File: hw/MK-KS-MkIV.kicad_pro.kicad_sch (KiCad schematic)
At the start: 88 parts, among them J1 MuKOB IF, J10 LOOP_CUR_LIMIT, J4 COMM-DCE-10, J5 RPi-GPIO40, J6 I2C Disp, J7 KEY-PADDLE, J8 LOOP PWR, J9 SNDR/KOB, Q1 G01N20LE, Q2 MMBT3904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

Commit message: Update manual. Add IF-MkIV.
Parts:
- removed D2 (x2): 1N4007, Diode_THT:D_DO-41_SOD81_P10.16mm_Horizontal, symbol Diode:1N4004
- removed Q3: 2N3904, Package_TO_SOT_THT:TO-92_Inline, symbol Transistor_BJT:2N3904
- removed Q3: MMBT3904, Package_TO_SOT_SMD:SOT-23, symbol Transistor_BJT:MMBT3904
- removed R2: 1k, Resistor_SMD:R_0805_2012Metric_Pad1.20x1.40mm_HandSolder, symbol Device:R_US
- added BT1: Battery_Cell, symbol Device:Battery_Cell
- added C7: 10uf Tant, Capacitor_Tantalum_SMD:CP_EIA-3528-12_Kemet-T_Pad1.50x2.35mm_HandSolder, symbol Device:C_Polarized_US
- added D1: HDS20M, AES_Library:AES-BridgeRect-HDS20M-13-1KV-2A, symbol Diode_Bridge:MB2S
- added D9: MBR180S1, Diode_SMD:D_SOD-123, symbol Diode:MBR0580
- added J7: KEY-PADDLE-1_8, AES_Library:CUI_SJ1-3534NG-audio-jack, symbol AES_Library:CUI_SJ1-3534NG-audio-jack
- added JP10: EX-PWR, Connector_PinHeader_2.54mm:PinHeader_1x02_P2.54mm_Vertical, symbol Jumper:Jumper_2_Open
- C10, C11, C12, C13, C8, C9, D3: Power (none) -> 100V
- C7: Power (none) -> 80V
- D5: Power (none) -> 1KV
- JP9: value KeyJack-NP -> Shield_GND
- R2: value 0 -> 0|16
- RLY1: renamed from MS1; value RELAY-3V-DPST -> RELAY-5v|3v-DPST
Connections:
- net SEB is gone; now on net SLG-C: SW4.3
- net +3.3V: no longer R2.1
- net +5V: now also D4.1 (K), R2.1, C7.1
- net GND: now also C7.2, D1.4 (-), J7.1, JP10.2 (B)
- net KEY_PDL-: now also J7.2
- net KOB_KEY-: now also J7.4
- net LOOP_PWR: now also D1.3 (+), JP10.1 (A)
- net LP2: now also D9.2 (A); no longer D4.2 (A)
- net PDL_DASH-: now also J7.3
- net SEL: now also LED1.1 (K), SW4.1; no longer R2.1, SW4.4
- net SNDR_EN: now also R2.1; no longer SW4.1, SW4.2
- net at Q1.3 (D): now also D9.1 (K); no longer D4.1 (K)
- net at U5.1 (SND): now also BT1.1 (+)
- net SLG-C: now reaches Q2.3 (C)
- net SLG-C: now also SW4.4; no longer LED1.1 (K)
- net SER: now reaches RLY1.A1
- net SER: now also D4.2 (A), SW4.2
- net LPI+ renamed LPI_A
- net LPI_A: now also D1.2
- net LPI- renamed LPI_B
- net LPI_B: now also D1.1
- no-connect marks 38 -> 39
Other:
- note added: "1/8in Key/Paddle Jack (Same as ICOM IC-9700)"
- note added: "FOR EXTERNALLY POWERED LOOP JUMPER JP10 (LOOP PWR)"
- note added: "IF EXTERNALLY POWERED - +"
- note added: "J3 (1/4in) or J7 (1/8in) are installed They occupy the same board area."
- note added: "Key/Paddle - Sounder Mini-Test"
- note added: "Normally connected. Remove to use the 'Test Key/Closer' (or keep external key open)"
- note added: "Use when J3/J7 not installed"
- note removed: "+ EXTERNALLY POWERED"
- note removed: "EXTERNALLY POWERED -"
- note removed: "FOR EXTERNALLY POWERED LOOP JUMPER J2 (LOOP PWR)"
- note removed: "Key/Paddle - Sounder DEBUG Remove JP2 to use."
- note removed: "Normally connected. Remove to use the 'Test Key/Closer'"
- note removed: "Use when J3 not installed"
- title: MuKOB / RPi / USB - KOB/Key/Paddle&Sounder IF MkIII -> MuKOB / RPi / USB - KOB/Key/Paddle&Sounder IF MkIV
- moved on the sheet: D4, J1, J8, JP7, LED1, M_KSI1, M_KSI2, M_KSI3, M_KSI4, OP1, Q2, R2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

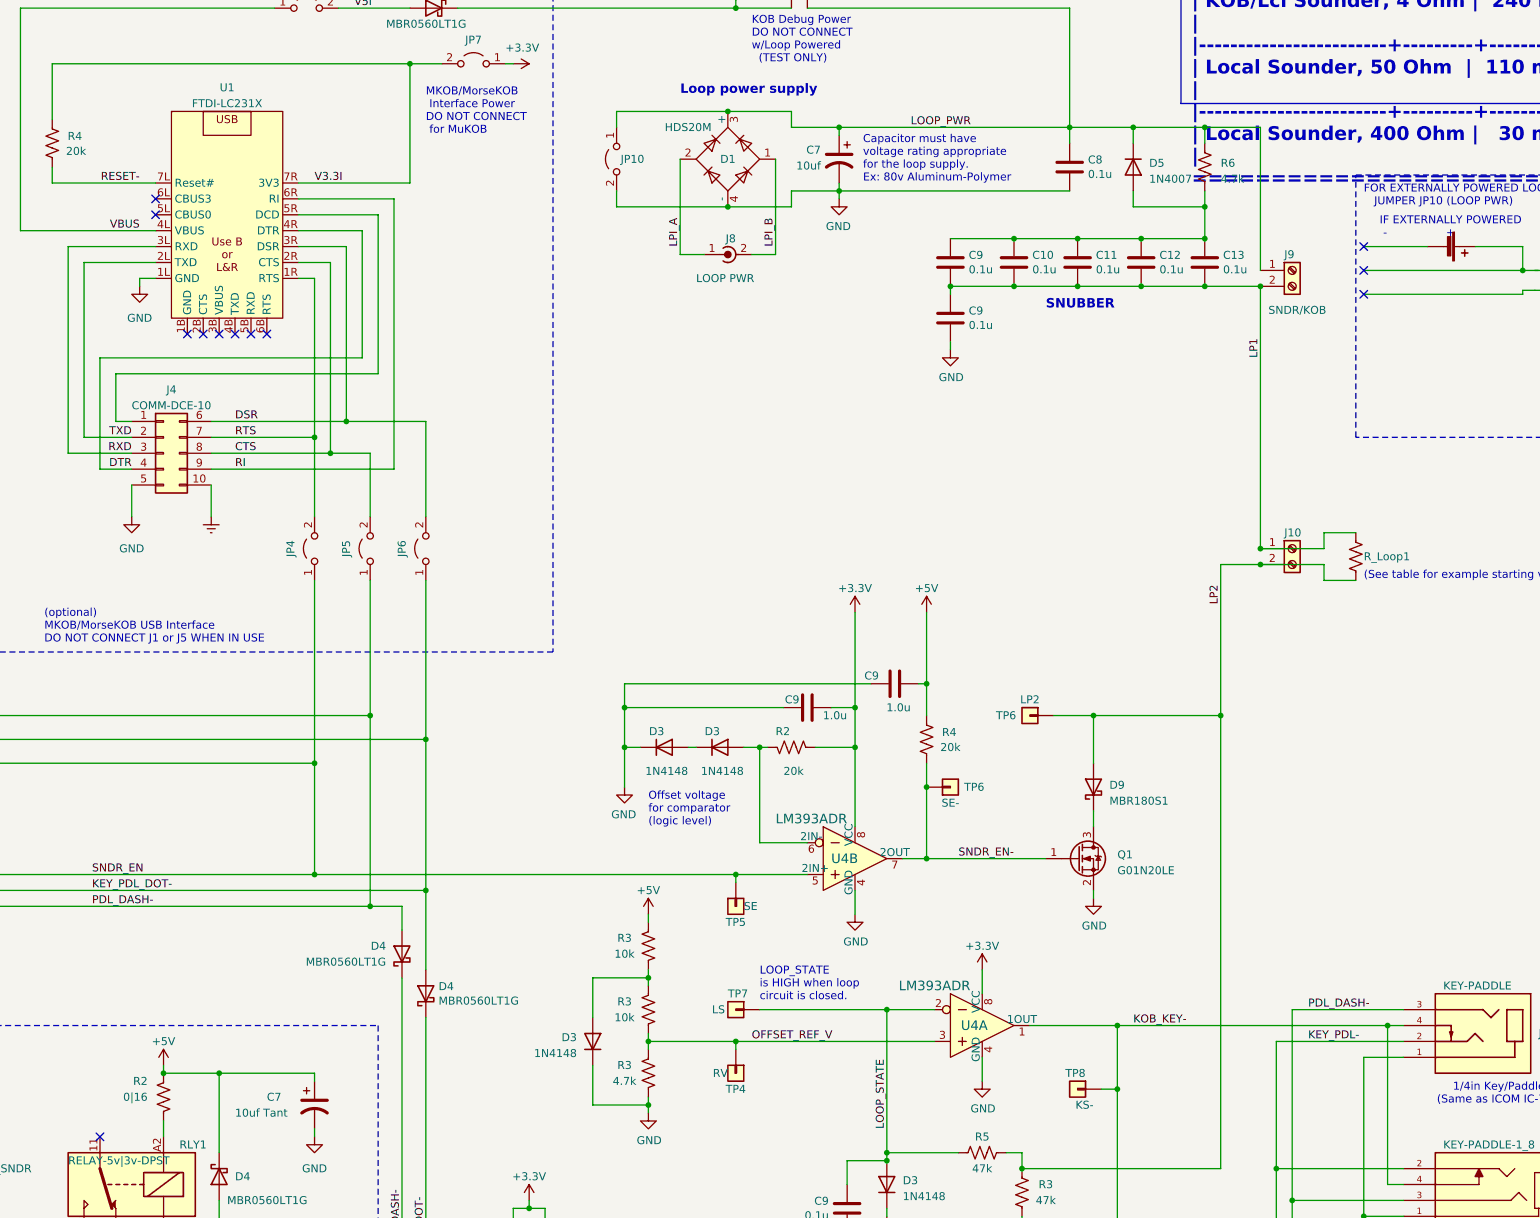
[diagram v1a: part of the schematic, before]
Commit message: KS-MkIV: Pinout for bridge and mini-sounder update.
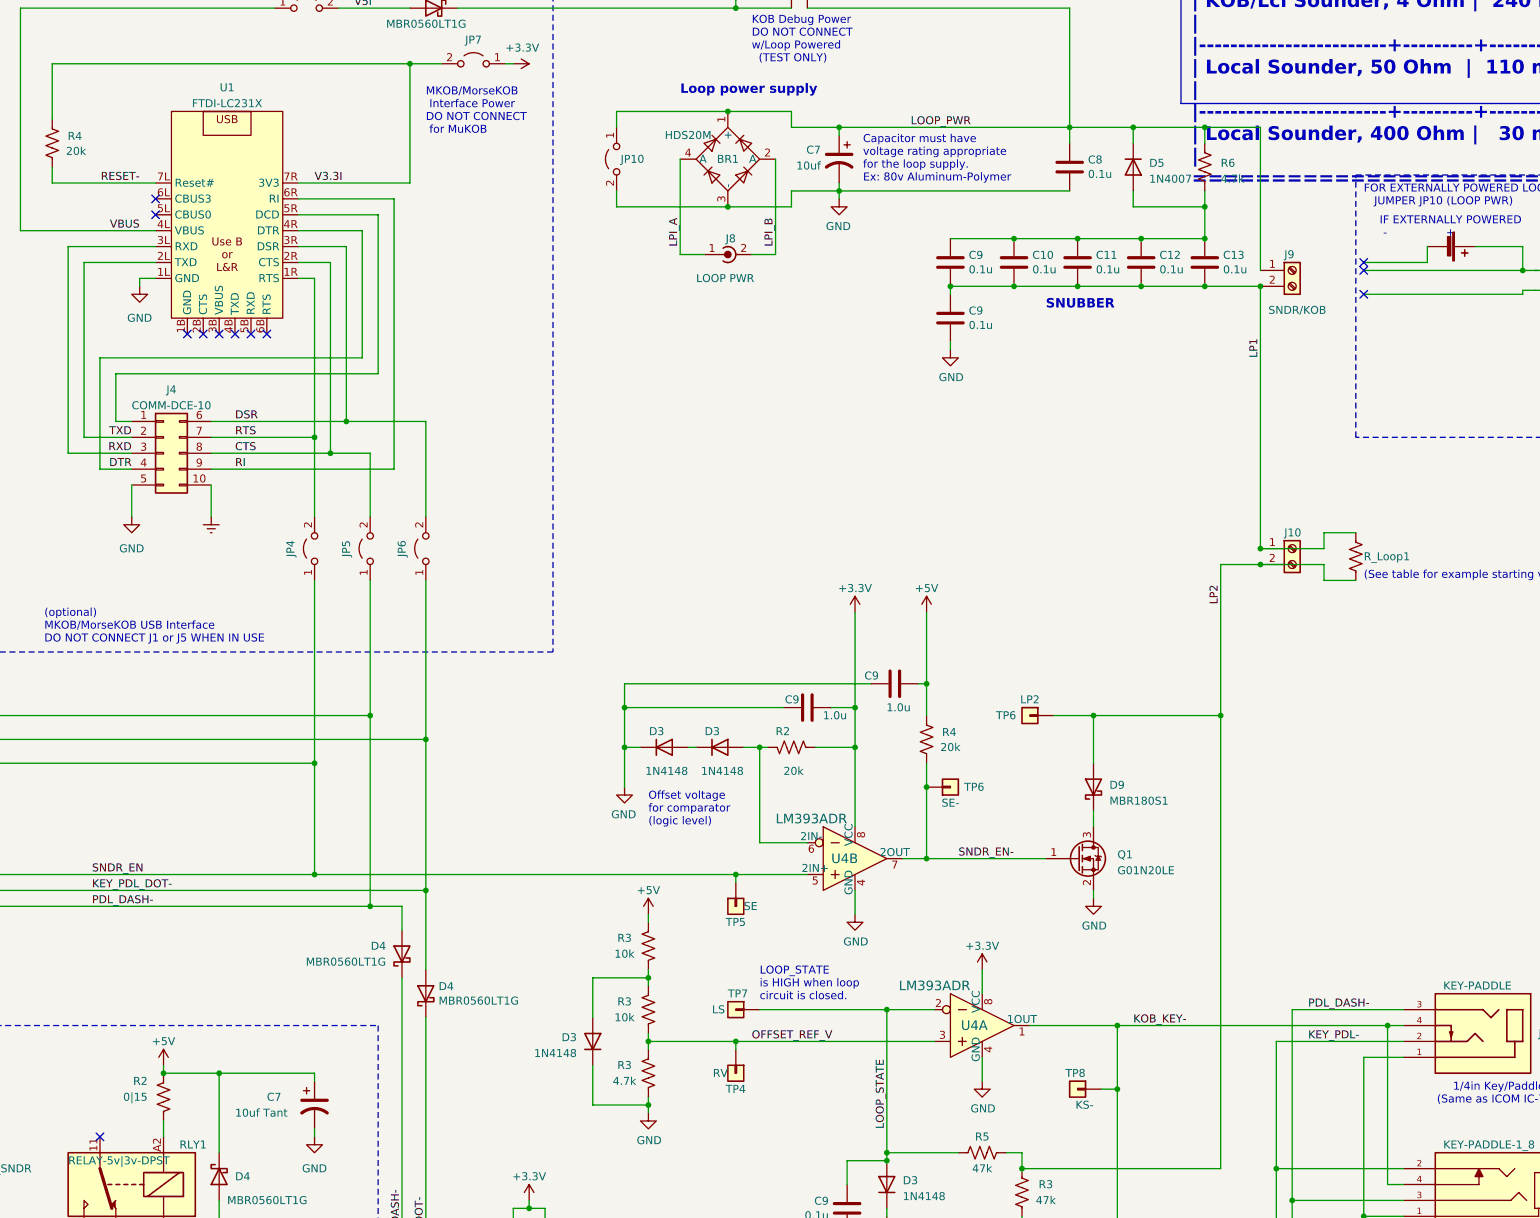
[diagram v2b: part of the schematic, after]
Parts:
- removed D1: HDS20M, AES_Library:AES-BridgeRect-HDS20M-13-1KV-2A, symbol Diode_Bridge:MB2S
- added BR1: HDS20M, AES_Library:AES-BridgeRect-HDS20M-13-1KV-2A, symbol AES_Library:AES-BridgeRect-HDS20M-13-1KV-2A
- R2: value 0|16 -> 0|15
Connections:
- net GND: now also BR1.3 (-)
- net LOOP_PWR: now also BR1.1 (+)
- net LPI_A: now also BR1.4 (A)
- net LPI_B: now also BR1.2 (A)
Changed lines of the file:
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@@
     (title "MuKOB / RPi / USB - KOB/Key/Paddle&Sounder IF MkIV")
     (date "2024-05-01")
-    (rev "1")
+    (rev "1.1")
     (company "Silky-Design (AESilky)")
     (comment 1 "Copyright 2023-24 AESilky")
@@
   (junction (at 251.46 170.18) (diameter 0) (color 0 0 0 0)
   )
+  (junction (at 193.04 88.9) (diameter 0) (color 0 0 0 0)
+  )
   (junction (at 271.78 170.18) (diameter 0) (color 0 0 0 0)
   )
@@
   (junction (at 180.34 222.25) (diameter 0) (color 0 0 0 0)
   )
-  (junction (at 193.04 88.9) (diameter 0) (color 0 0 0 0)
-  )
   (junction (at 269.24 93.98) (diameter 0) (color 0 0 0 0)
   )
@@
   (junction (at 274.32 289.56) (diameter 0) (color 0 0 0 0)
   )
-  (junction (at 193.04 73.66) (diameter 0) (color 0 0 0 0)
-  )
   (junction (at 224.79 181.61) (diameter 0) (color 0 0 0 0)
   )
@@
   (junction (at 140.97 269.24) (diameter 0) (color 0 0 0 0)
   )
+  (junction (at 193.04 73.66) (diameter 0) (color 0 0 0 0)
+  )
   (junction (at 176.53 168.91) (diameter 0) (color 0 0 0 0)
   )
@@
   (no_connect (at 60.96 118.11))
   (no_connect (at 109.22 109.22))
-  (no_connect (at 294.64 95.25))
+  (no_connect (at 294.64 97.79))
   (no_connect (at 30.48 102.87))
   (no_connect (at 30.48 130.81))
@@
     (stroke (width 0) (type default))
   )
-  (wire (pts (xy 193.04 88.9) (xy 203.2 88.9))
+  (wire (pts (xy 175.26 88.9) (xy 193.04 88.9))
     (stroke (width 0) (type default))
   )
@@
     (stroke (width 0) (type default))
   )
+  (wire (pts (xy 193.04 88.9) (xy 203.2 88.9))
+    (stroke (width 0) (type default))
+  )
   (wire (pts (xy 60.96 138.43) (xy 68.58 138.43))
     (stroke (width 0) (type default))
@@
     (stroke (width 0) (type default))
   )
+  (wire (pts (xy 193.04 73.66) (xy 203.2 73.66))
+    (stroke (width 0) (type default))
+  )
   (wire (pts (xy 20.32 177.8) (xy 127 177.8))
     (stroke (width 0) (type default))
@@
     (stroke (width 0) (type default))
   )
-  (wire (pts (xy 175.26 88.9) (xy 193.04 88.9))
-    (stroke (width 0) (type default))
-  )
   (wire (pts (xy 288.29 148.59) (xy 288.29 146.05))
     (stroke (width 0) (type default))
@@
     (stroke (width 0) (type default))
   )
-  (wire (pts (xy 294.64 95.25) (xy 304.8 95.25))
+  (wire (pts (xy 294.64 97.79) (xy 304.8 97.79))
     (stroke (width 0) (type default))
   )
@@
     (stroke (width 0) (type default))
   )
+  (wire (pts (xy 304.8 97.79) (xy 304.8 95.25))
+    (stroke (width 0) (type default))
+  )
   (wire (pts (xy 271.78 170.18) (xy 271.78 242.57))
     (stroke (width 0) (type default))
@@
     (stroke (width 0) (type default))
   )
-  (wire (pts (xy 193.04 73.66) (xy 203.2 73.66))
-    (stroke (width 0) (type default))
-  )
   (wire (pts (xy 125.73 298.45) (xy 140.97 298.45))
     (stroke (width 0) (type default))
@@
   (rectangle (start 293.37 83.82) (end 382.905 125.73)
     (stroke (width 0) (type dash) (color 255 0 0 1))
-    (fill (type color) (color 194 194 194 0.1))
+    (fill (type none))
   )
   (rectangle (start 76.2 52.07) (end 165.1 160.02)
@@
     )
   )
+  (symbol (lib_id "AES_Library:AES-BridgeRect-HDS20M-13-1KV-2A") (at 193.04 81.28 90) (unit 1)
+    (in_bom yes) (on_board yes) (dnp no)
+    (property "Reference" "BR1" (at 193.04 81.28 90)
+      (effects (font (size 1.27 1.27)))
+    )
+    (property "Value" "HDS20M" (at 186.69 77.47 90)
+      (effects (font (size 1.27 1.27)))
+    )
+    (property "Footprint" "AES_Library:AES-BridgeRect-HDS20M-13-1KV-2A" (at 193.04 81.28 0)
+      (effects (font (size 1.27 1.27)) hide)
+    )
+    (property "Datasheet" "https://www.diodes.com/assets/Datasheets/HDS20M.pdf" (at 193.04 81.28 0)
+      (effects (font (size 1.27 1.27)) hide)
+    )
+    (pin "1")
+    (pin "2")
+    (pin "3")
+    (pin "4")
+    (instances
+      (project "MK-KS-MkIV.kicad_pro"
+        (path "/c58d90c2-85f3-4e69-91d5-1bcb030f2211"
+          (reference "BR1") (unit 1)
+        )
+      )
+    )
+  )
   (symbol (lib_id "Device:R_US") (at 293.37 144.78 0) (unit 1)
     (in_bom no) (on_board no) (dnp no)
@@
     )
   )
-  (symbol (lib_id "Diode_Bridge:MB2S") (at 193.04 81.28 90) (unit 1)
-    (in_bom yes) (on_board yes) (dnp no)
-    (property "Reference" "D1" (at 193.04 81.28 90)
-      (effects (font (size 1.27 1.27)))
-    )
-    (property "Value" "HDS20M" (at 186.69 76.2 90)
-      (effects (font (size 1.27 1.27)))
-    )
-    (property "Footprint" "AES_Library:AES-BridgeRect-HDS20M-13-1KV-2A" (at 189.865 77.47 0)
-      (effects (font (size 1.27 1.27)) (justify left) hide)
-    )
-    (property "Datasheet" "http://www.vishay.com/docs/88661/mb2s.pdf" (at 193.04 81.28 0)
-      (effects (font (size 1.27 1.27)) hide)
-    )
-    (pin "1")
-    (pin "2")
-    (pin "3")
-    (pin "4")
-    (instances
-      (project "MK-KS-MkIV.kicad_pro"
-        (path "/c58d90c2-85f3-4e69-91d5-1bcb030f2211"
-          (reference "D1") (unit 1)
-        )
-      )
-    )
-  )
   (symbol (lib_id "Connector:Screw_Terminal_01x02") (at 283.21 143.51 0) (unit 1)
     (in_bom yes) (on_board yes) (dnp no)
@@
       (effects (font (size 1.27 1.27)) (justify left))
     )
-    (property "Value" "0|16" (at 100.33 231.14 0)
+    (property "Value" "0|15" (at 100.33 231.14 0)
       (effects (font (size 1.27 1.27)) (justify left))
     )
